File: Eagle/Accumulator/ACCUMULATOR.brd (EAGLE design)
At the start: 100 x 100 mm, 12 parts

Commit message: worked on accumulator
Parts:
- added LED0, LED1, LED10, LED11, LED12, LED13, LED14, LED15, LED2, LED3, LED4, LED5, LED6, LED7, LED8, LED9, SC_000, SC_400, SC_800: (no value), led:LED3MM
- added R0, R1, R10, R11, R12, R13, R14, R15, R2, R3, R4, R5, R6, R7, R8, R9, RSC_000, RSC_400, RSC_800: (no value), rcl:0204/7
- moved SKIPCOND 8.00 mm to (7.62, 84.2)
- moved ACC=0_0-7 7.00 mm to (95.7, 92.0)
- moved ACCUMULATOR_0-7 7.00 mm to (96.7, 52.7)
- moved ACCUMULATOR_8-15 7.00 mm to (59.6, 52.5)
- moved ACO_0-7 7.00 mm to (84.8, 27.4)
- moved ACO_8-15 7.00 mm to (47.8, 27.9)
- moved AND_GATE 7.00 mm to (92.2, 69.4)
- moved NOT_GATE 7.00 mm to (68.0, 68.4)
- moved TRIPLE_AND_GATE 7.00 mm to (39.0, 69.4)
- moved ACC=0_8-15 7.00 mm to (64.7, 92.0)
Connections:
- new net N$10: RSC_000.2, SC_000.A
- new net N$11: LED0.K, LED1.K, LED10.K, LED11.K, LED12.K, LED13.K, LED14.K, LED15.K, LED2.K, LED3.K, LED4.K, LED5.K, LED6.K, LED7.K, LED8.K, LED9.K
- new net N$14: LED1.A, R1.1
- new net N$16: LED2.A, R2.1
- new net N$18: LED3.A, R3.1
- new net N$19: LED4.A, R4.1
- new net N$2: RSC_800.2, SC_800.A
- new net N$20: LED5.A, R5.1
- new net N$21: LED6.A, R6.1
- new net N$22: LED7.A, R7.1
- new net N$23: LED8.A, R8.1
- new net N$24: LED9.A, R9.1
- new net N$25: LED10.A, R10.1
- new net N$26: LED11.A, R11.1
- new net N$27: LED12.A, R12.1
- new net N$28: LED13.A, R13.1
- new net N$29: LED14.A, R14.1
- new net N$3: RSC_400.2, SC_400.A
- new net N$30: LED15.A, R15.1
- new net N$31: LED0.A, R0.1
- net AC0: now also R0.2
- net AC1: now also R1.2
- net AC10: now also R10.2
- net AC11: now also R11.2
- net AC12: now also R12.2
- net AC13: now also R13.2
- net AC14: now also R14.2
- net AC15: now also R15.2
- net AC2: now also R2.2
- net AC3: now also R3.2
- net AC4: now also R4.2
- net AC5: now also R5.2
- net AC6: now also R6.2
- net AC7: now also R7.2
- net AC8: now also R8.2
- net AC9: now also R9.2
- net GND: now also SC_000.K, SC_400.K, SC_800.K, SKIPCOND.5, SKIPCOND.6, SKIPCOND.7, SKIPCOND.8, SKIPCOND.9
- net N$17: now also RSC_800.1
- net N$8: now also RSC_400.1
- net N$9: now also RSC_000.1

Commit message: Added input to logisim and worked on IR
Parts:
- moved R15 220.5 mm to (31.0, 80.0)
- moved R14 211.6 mm to (31.0, 75.0)
- moved R13 202.7 mm to (31.0, 70.0)
- moved R12 193.8 mm to (31.0, 65.0)
- moved R11 184.8 mm to (31.0, 60.0)
- moved R10 175.9 mm to (31.0, 55.0)
- moved R9 167.0 mm to (31.0, 50.0)
- moved R8 158.2 mm to (31.0, 45.0)
- moved LED15 153.8 mm to (19.0, 80.0)
- moved R0 150.3 mm to (31.0, 5.00)
- moved R7 149.3 mm to (31.0, 40.0)
- moved LED14 143.9 mm to (19.0, 75.0)
- moved R6 140.4 mm to (31.0, 35.0)
- moved LED13 134.0 mm to (19.0, 70.0)
- moved R5 131.6 mm to (31.0, 30.0)
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
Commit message: finished most boards
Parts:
- added C1, C2, C3, C4: (no value), rcl:C025-024X044
- added U$1, U$2, U$3, U$4: (no value), holes:2,8
- moved SC_000 96.0 mm to (70.0, 15.0), turned to 180 degrees
- moved SC_400 96.0 mm to (70.0, 10.0), turned to 180 degrees
- moved SC_800 96.0 mm to (70.0, 5.00), turned to 180 degrees
- moved RSC_000 93.8 mm to (86.0, 14.0)
- moved RSC_400 93.8 mm to (86.0, 10.0)
- moved RSC_800 93.8 mm to (86.0, 6.00)
- moved LED0 76.4 mm to (93.0, 24.0), turned to 270 degrees
- moved LED1 70.4 mm to (88.0, 24.0), turned to 270 degrees
- moved R0 68.4 mm to (93.0, 34.0), turned to 90 degrees
- moved LED2 64.6 mm to (83.0, 24.0), turned to 270 degrees
- moved ACO_0-7 62.2 mm to (36.5, 66.8), turned to 180 degrees
- moved R1 61.8 mm to (88.0, 34.0), turned to 90 degrees
- moved LED3 59.1 mm to (78.0, 24.0), turned to 270 degrees
- moved LED15 56.0 mm to (18.0, 24.0), turned to 270 degrees
- moved R2 55.4 mm to (83.0, 34.0), turned to 90 degrees
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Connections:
- net GND: now also C1.1, C2.1, C3.1, C4.1
- net VCC: now also C1.2, C2.2, C3.2, C4.2
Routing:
- net GND: track 0.00 -> 463.1 mm, vias 0 -> 1
- net VCC: track 0.00 -> 283.1 mm, vias 0 -> 3
- net AC2: track 0.00 -> 223.8 mm, vias 0 -> 2
- net AC12: track 0.00 -> 205.8 mm, vias 0 -> 3
- net B3: track 0.00 -> 203.5 mm, vias 0 -> 5
- net AC3: track 0.00 -> 195.8 mm, vias 0 -> 3
- net AC1: track 0.00 -> 192.6 mm, vias 0 -> 2
- net AC14: track 0.00 -> 188.3 mm, vias 0 -> 2
- net B4: track 0.00 -> 180.8 mm, vias 0 -> 4
- net B11: track 0.00 -> 179.4 mm, vias 0 -> 5
- net N$17: track 0.00 -> 178.4 mm, vias 0 -> 2
- net B2: track 0.00 -> 177.3 mm, vias 0 -> 4
- net AC0: track 0.00 -> 176.9 mm, vias 0 -> 3
- net AC11: track 0.00 -> 170.4 mm, vias 0 -> 6
- net AC5: track 0.00 -> 169.7 mm, vias 0 -> 3
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
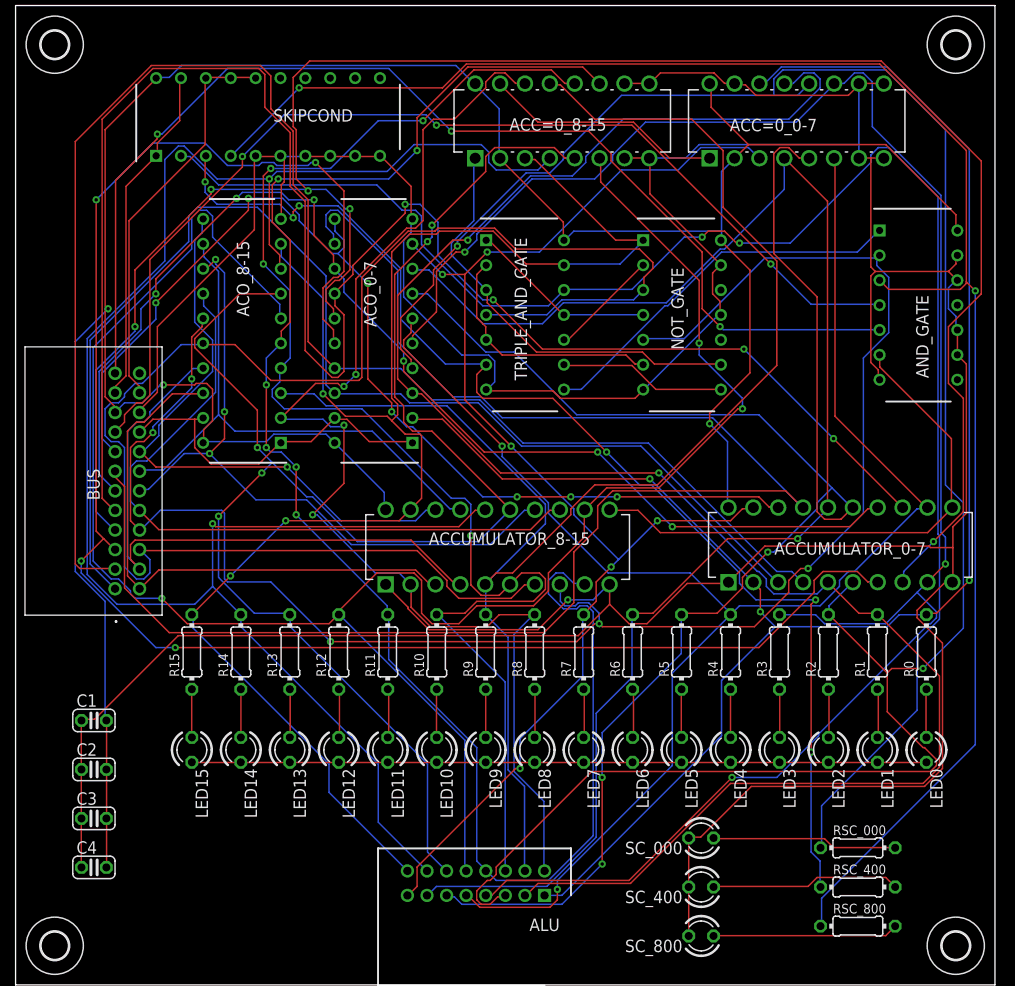
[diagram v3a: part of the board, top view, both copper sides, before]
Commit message: added Clock
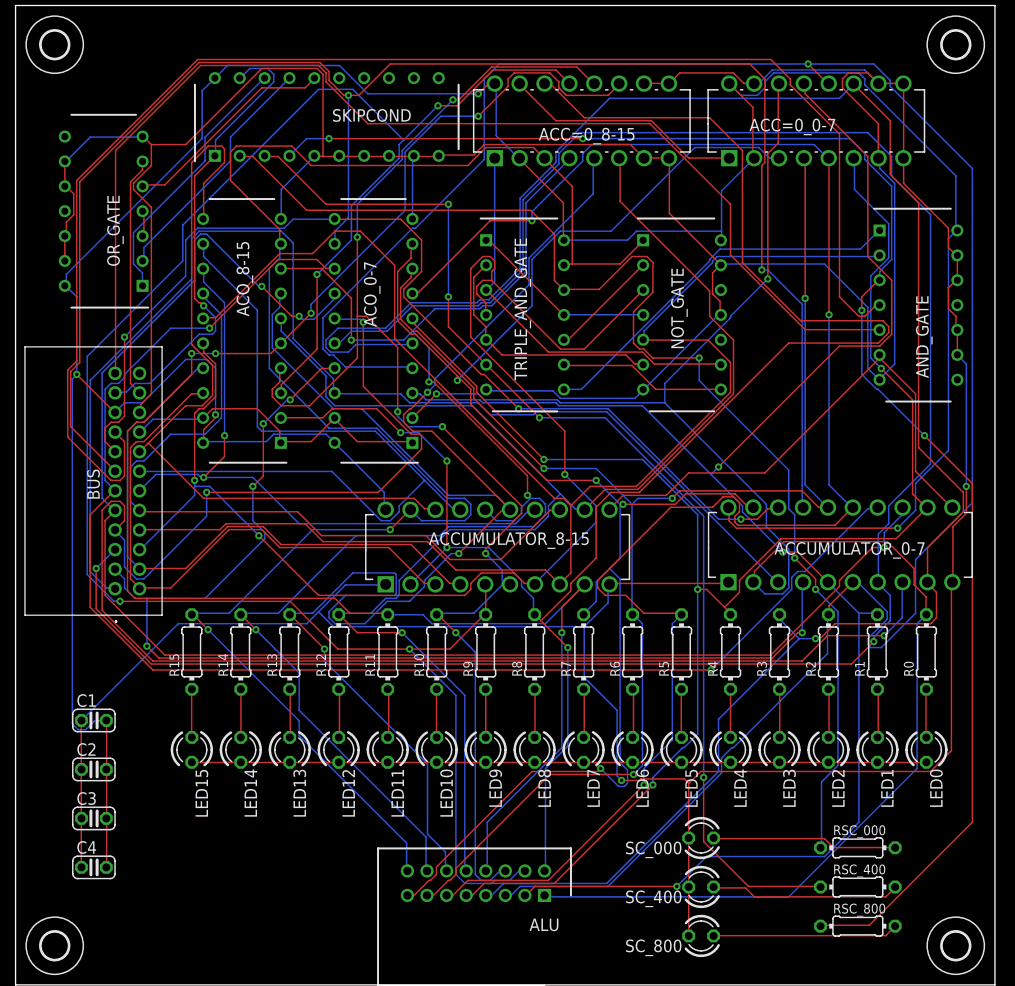
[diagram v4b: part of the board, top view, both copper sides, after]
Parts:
- added OR_GATE: SN74HC32N, SamacSys_Parts:DIP794W53P254L1930H508Q14N
- moved SKIPCOND 6.00 mm to (31.8, 88.6)
- moved ACC=0_0-7 2.00 mm to (90.7, 92.0)
- moved ACC=0_8-15 2.00 mm to (66.7, 92.0)
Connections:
- new net N$32: OR_GATE.1, SKIPCOND.18
- new net N$33: OR_GATE.2, SKIPCOND.17
- new net N$34: OR_GATE.3, OR_GATE.4
- new net N$35: OR_GATE.5, SKIPCOND.16
- net CE: now also OR_GATE.6; no longer SKIPCOND.16, SKIPCOND.17, SKIPCOND.18
- net GND: now also OR_GATE.10, OR_GATE.12, OR_GATE.13, OR_GATE.7, OR_GATE.9
- net VCC: now also OR_GATE.14
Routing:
- net AC8: track 126.7 -> 179.2 mm
- net AC12: track 205.8 -> 153.6 mm, vias 3 -> 1
- net AC9: track 157.6 -> 203.0 mm, vias 0 -> 4
- net GND: track 463.1 -> 508.0 mm, vias 1 -> 2
- net N$9: track 167.2 -> 125.3 mm, vias 2 -> 3
- net AC14: track 188.3 -> 147.9 mm, vias 2 -> 4
- net B1: track 160.4 -> 120.4 mm, vias 0 -> 5
- net ACI: track 108.7 -> 147.8 mm, vias 3 -> 0
- net B2: track 177.3 -> 215.8 mm, vias 4 -> 2
- net B3: track 203.5 -> 166.2 mm, vias 5 -> 3
- net VCC: track 283.1 -> 313.8 mm, vias 3 -> 4
- net B4: track 180.8 -> 152.6 mm, vias 4 -> 3
- net AC7: track 137.7 -> 165.5 mm, vias 6 -> 4
- net N$32: track 0.00 -> 27.2 mm
- net N$33: track 0.00 -> 24.9 mm
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
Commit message: added gerber files for each board
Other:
- board text added: "MARIE PC Accumulator Architecture design by: Dr. Linda Null Hardware implementation by: Richard Bowser"
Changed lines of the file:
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@@
 <wire x1="100" y1="100" x2="0" y2="100" width="0" layer="20"/>
 <wire x1="0" y1="100" x2="0" y2="0" width="0" layer="20"/>
+<text x="75" y="72" size="1.778" layer="26" rot="MR0">MARIE PC
+Accumulator
+Architecture design by: Dr. Linda Null
+Hardware implementation by: Richard Bowser</text>
 </plain>
 <attributes>
@@
 </drawing>
 <compatibility>
+<note version="6.3" minversion="6.2.2" severity="warning">
+Since Version 6.2.2 text objects can contain more than one line,
+which will not be processed correctly with this version.
+</note>
 <note version="8.2" severity="warning">
 Since Version 8.2, EAGLE supports online libraries. The ids

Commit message: started adding revision 2 to fix errors in first set of boards
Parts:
- LED0, LED1, LED10, LED11, LED12, LED13, LED14, LED15, LED2, LED3, LED4, LED5, LED6, LED7, LED8, LED9: value (none) -> RED
- R0, R1, R10, R11, R12, R13, R14, R15, R2, R3, R4, R5, R6, R7, R8, R9, RSC_000, RSC_400, RSC_800: value (none) -> 220
- SC_000, SC_400, SC_800: value (none) -> YELLOW
